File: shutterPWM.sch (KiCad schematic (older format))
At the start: 25 parts, among them P11 2x3 header strip R/A, P12 2x3 header strip R/A, U2 DRV103, U3 DRV103, U4 MCP4728

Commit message: Fixed PCB routing
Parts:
- D5, D6: footprint (none) -> Diodes_SMD:SOD-323
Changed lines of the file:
@@
 LIBS:valves
 LIBS:jakub
-LIBS:MicroFLiC_servo_solenoid-cache
+LIBS:MicroFLiC_servo_solenoid_bottom-cache
 EELAYER 25 0
 EELAYER END
@@
 F 0 "D5" H 5100 2200 50  0000 C CNN
 F 1 "1N4148" H 5100 2400 50  0000 C CNN
-F 2 "" H 5100 2300 50  0000 C CNN
+F 2 "Diodes_SMD:SOD-323" H 5100 2300 50  0001 C CNN
 F 3 "" H 5100 2300 50  0000 C CNN
 F 4 "1N4148WS" H 5100 2300 60  0001 C CNN "Part Number"
@@
 F 0 "D6" H 5100 5400 50  0000 C CNN
 F 1 "1N4148" H 5100 5600 50  0000 C CNN
-F 2 "" H 5100 5500 50  0000 C CNN
+F 2 "Diodes_SMD:SOD-323" H 5100 5500 50  0001 C CNN
 F 3 "" H 5100 5500 50  0000 C CNN
 F 4 "1N4148WS" H 5100 5500 60  0001 C CNN "Part Number"

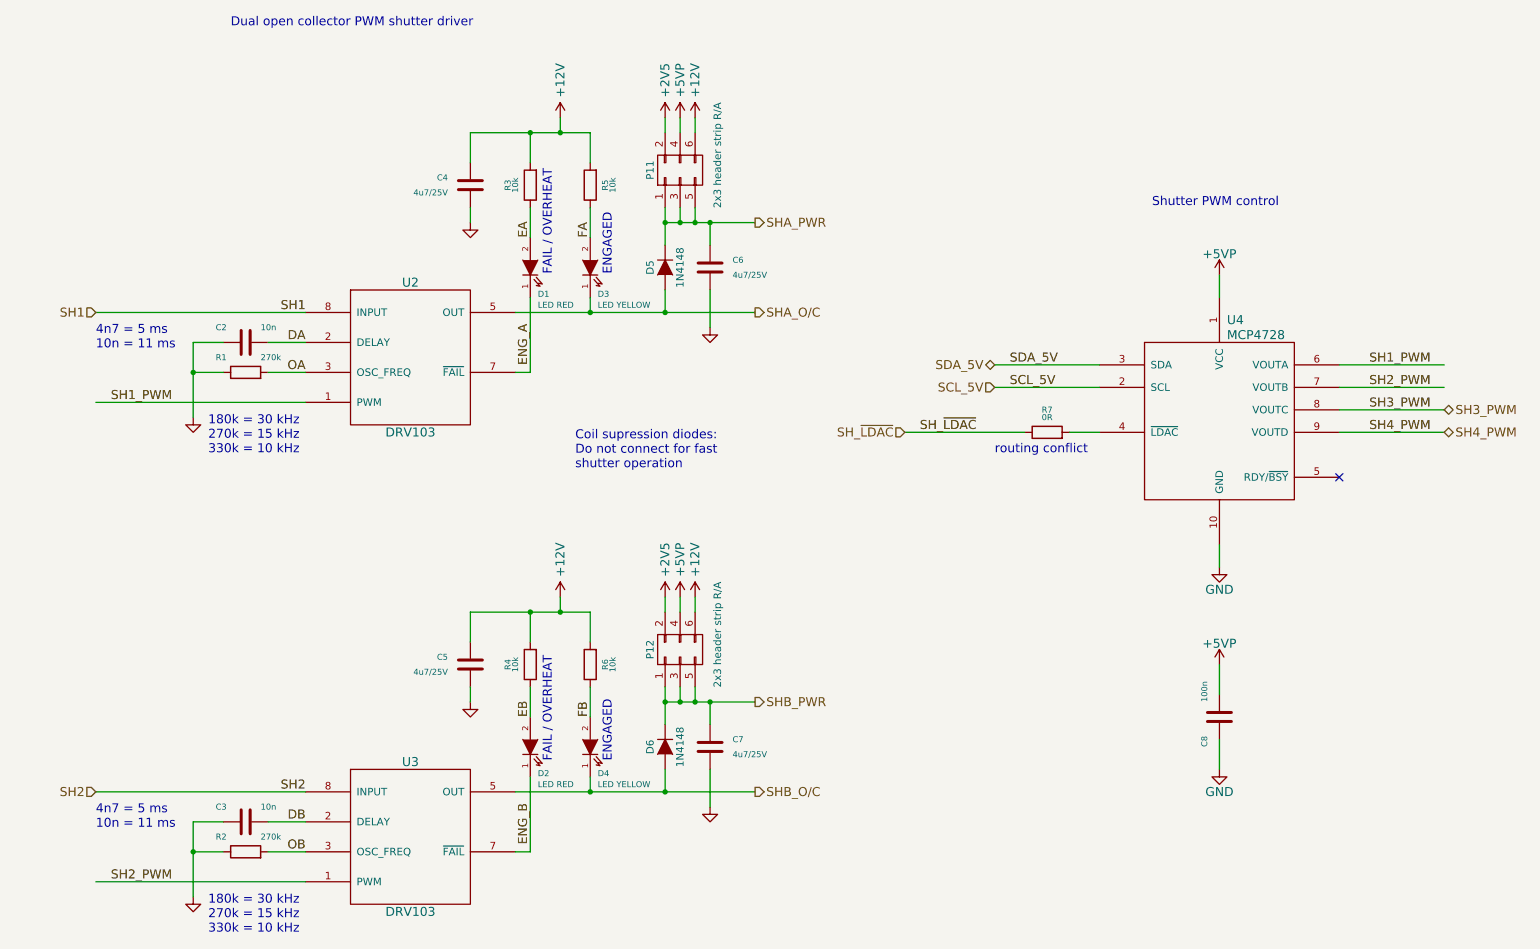
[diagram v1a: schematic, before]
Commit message: Created v1.1, got rid of all redundant parts for separate top and bottom boards
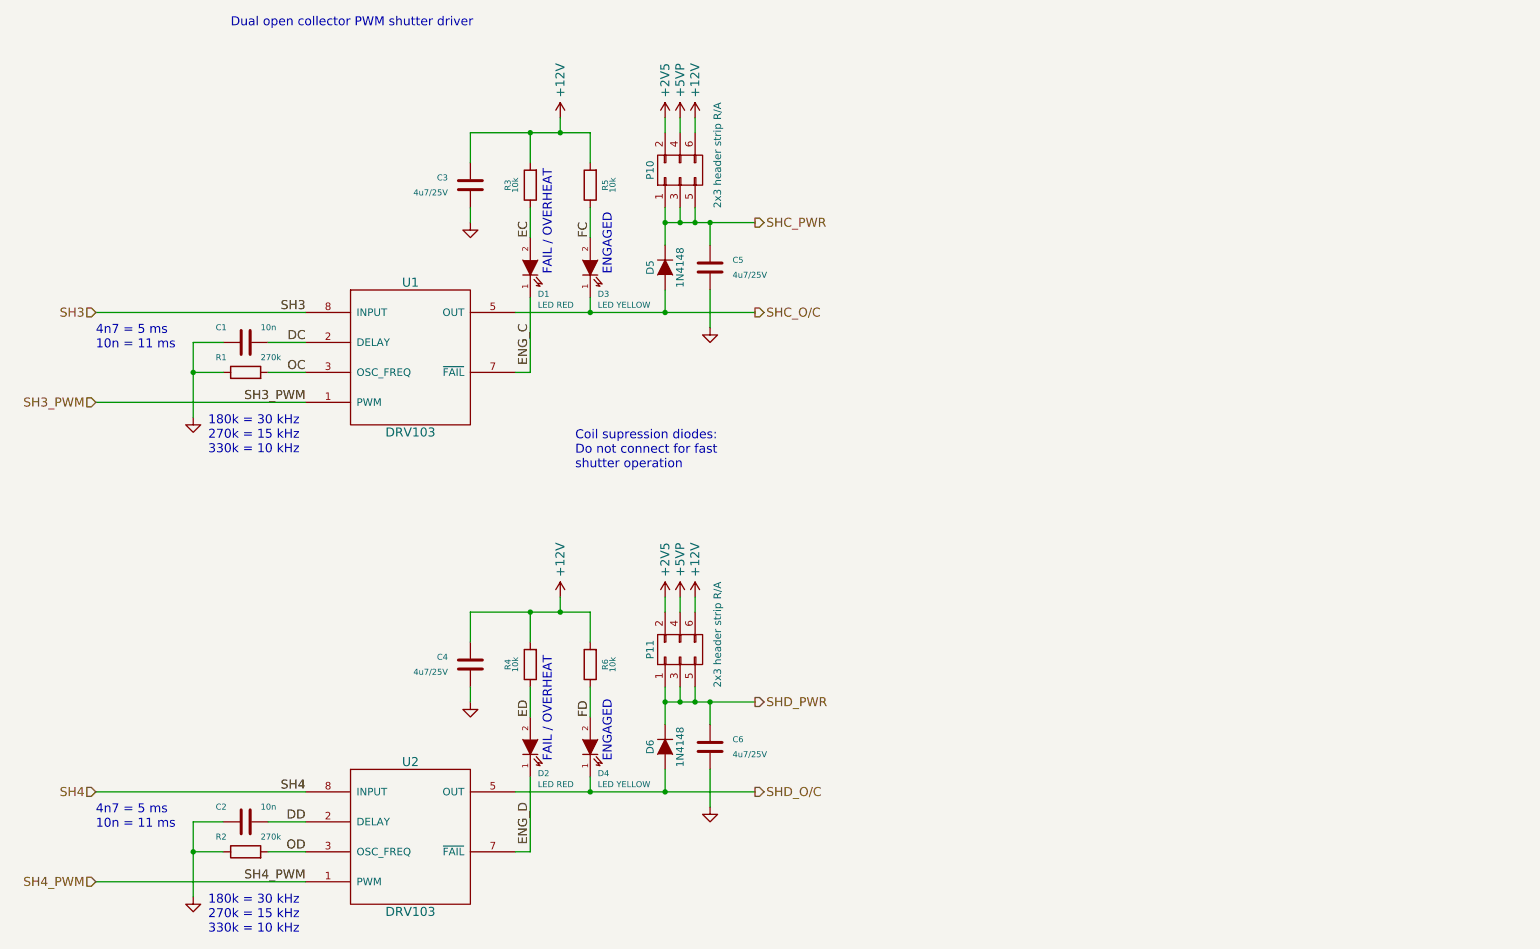
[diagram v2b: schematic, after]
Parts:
- removed C8: 100n, Capacitors_SMD:C_0805, symbol C
- removed R7: 0R, Resistors_SMD:R_0805, symbol R
- removed U4: MCP4728, Housings_SSOP:MSOP-10_3x3mm_Pitch0.5mm, symbol MCP4728
- renumbered C2 to C1, C3 to C2, C4 to C3, C5 to C4, C6 to C5, C7 to C6, P11 to P10, P12 to P11, U2 to U1, U3 to U2
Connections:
- net labels added: DC, DD, EC, ED, ENG_C, ENG_D, FC, FD, OC, OD, SH3, SH4, SHC_O/C, SHC_PWR, SHD_O/C, SHD_PWR
- net labels removed: DA, DB, EA, EB, ENG_A, ENG_B, FA, FB, OA, OB, SCL_5V, SDA_5V, SH1, SH1_PWM, SH2, SH2_PWM, SHA_O/C, SHA_PWR, SHB_O/C, SHB_PWR, SH_~LDAC
- wire segments 70 -> 58
- no-connect marks 1 -> 0
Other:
- note removed: "Shutter PWM control"
- note removed: "routing conflict"
